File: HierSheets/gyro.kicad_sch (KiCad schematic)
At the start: 0 parts

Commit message: .
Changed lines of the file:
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@@
 	(generator_version "10.0")
 	(paper "A4")
+	(bus_entry
+		(at 0.0763 14.0462)
+		(size 2.54 -2.54)
+		(stroke
+			(width 0)
+			(type default)
+		)
+	)
+	(bus_entry
+		(at 0.0763 16.5862)
+		(size 2.54 -2.54)
+		(stroke
+			(width 0)
+			(type default)
+		)
+	)
 	(wire
 		(pts
-			(xy 143.51 107.95) (xy 143.51 92.71)
+			(xy 3.8863 0.0762) (xy 3.8863 12.7762)
 		)
 		(stroke
@@
 	(wire
 		(pts
-			(xy 140.97 107.95) (xy 143.51 107.95)
+			(xy 2.6163 14.0462) (xy 3.8863 12.7762)
 		)
 		(stroke
@@
 	(wire
 		(pts
-			(xy 143.51 92.71) (xy 148.59 92.71)
+			(xy 2.6163 0.0762) (xy 2.6163 11.5062)
 		)
 		(stroke

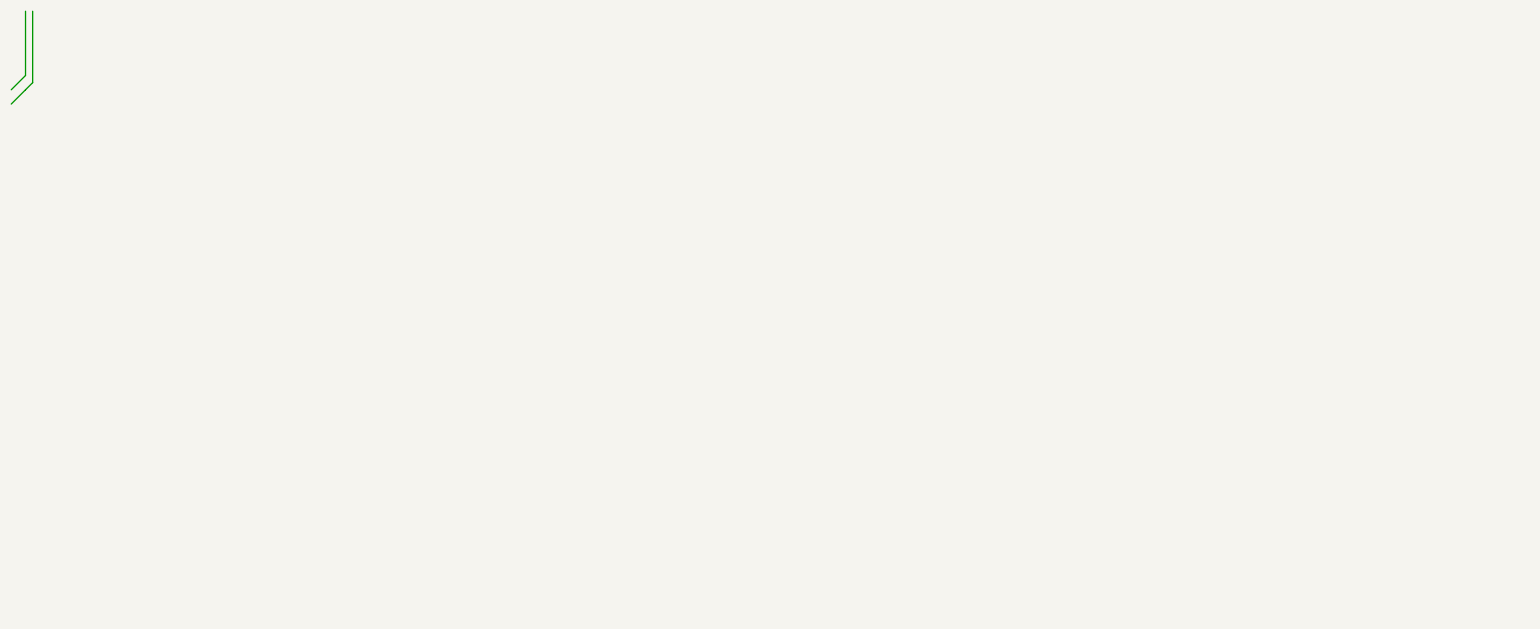
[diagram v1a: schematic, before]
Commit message: Added kicker, interrupt, I2C pullups, buck converter, button
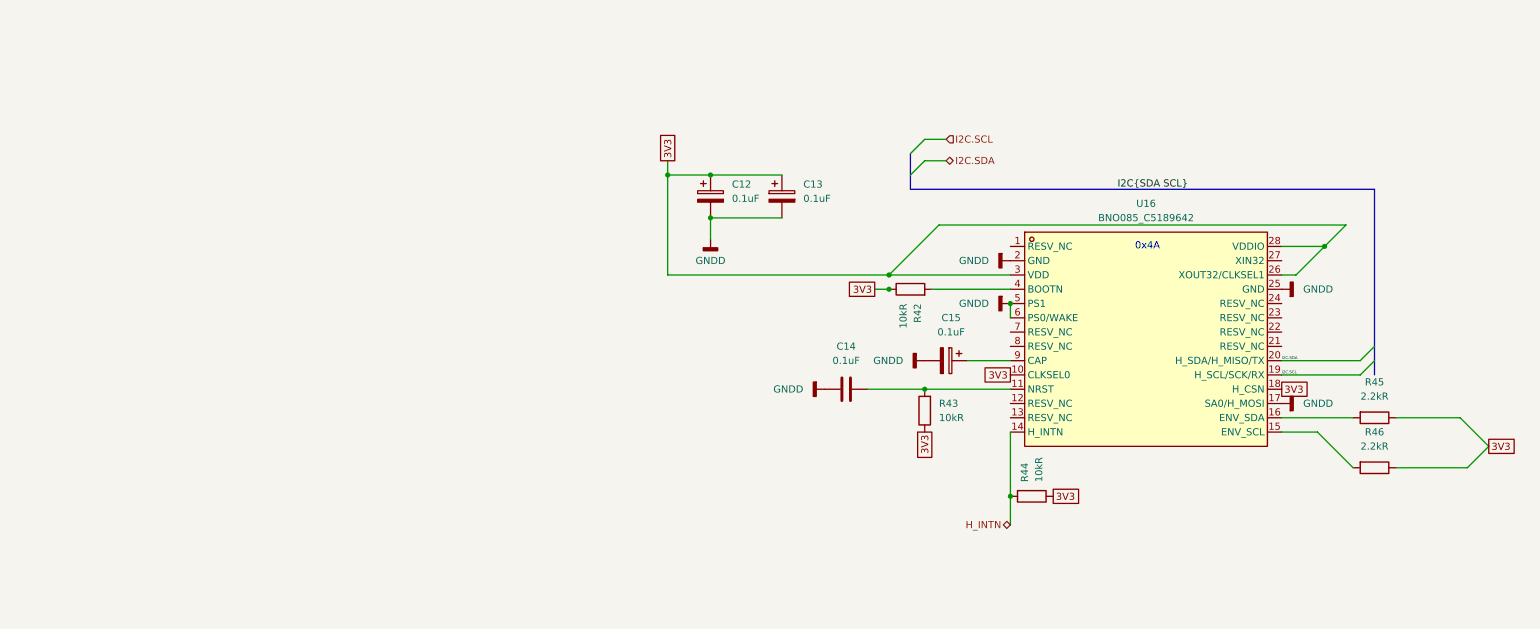
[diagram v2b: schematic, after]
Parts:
- added C12, C13, C15: 0.1uF, symbol Device:C_Polarized
- added C14: 0.1uF, symbol Device:C
- added R42, R43, R44: 10kR, symbol Device:R
- added R45, R46: 2.2kR, symbol Device:R
- added U16: BNO085_C5189642, easyeda2kicad:LGA-28_L5.2-W3.8-P0.50-BL, symbol EasyEDA2Kicad:BNO085_C5189642
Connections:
- new net: R46.2, U16.15 (ENV_SCL)
- new net: R45.2, U16.16 (ENV_SDA)
- new net: C14.2, R43.2, U16.11 (NRST)
- new net: R42.2, U16.4 (BOOTN)
- new net: C15.1, U16.9 (CAP)
- new net 3V3: C12.1, C13.1, R42.1, R43.1, R44.1, R45.1, R46.1, U16.10 (CLKSEL0), U16.18 (H_CSN), U16.26 (XOUT32/CLKSEL1), U16.28 (VDDIO), U16.3 (VDD)
- new net GNDD: C12.2, C13.2, C14.1, C15.2, U16.17 (SA0/H_MOSI), U16.2 (GND), U16.25 (GND), U16.5 (PS1), U16.6 (PS0/WAKE)
- new net H_INTN: R44.2, U16.14 (H_INTN)
- new net I2C.SCL: U16.19 (H_SCL/SCK/RX)
- new net I2C.SDA: U16.20 (H_SDA/H_MISO/TX)
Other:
- note added: "0x4A"
